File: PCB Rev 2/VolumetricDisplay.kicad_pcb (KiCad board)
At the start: 4 copper layers, 48.5 x 56 mm, 149 parts, among them J1 USB_C_Receptacle_USB2.0_16P, J2 Conn_ARM_SWD_TagConnect_TC2030, Q1 DMN32D2LDF, Q2 DMN32D2LDF, Q3 DMN32D2LDF, Q4 DMN32D2LDF, SW4 TS-1088-AR02016, SW5 TS-1088-AR02016, U2 NCP718xSN330, U3 RP2354B, U4 DRV8311S, U5 DRV5055A1xDBZxQ1, Y1 Abracon ABM8-272-T3

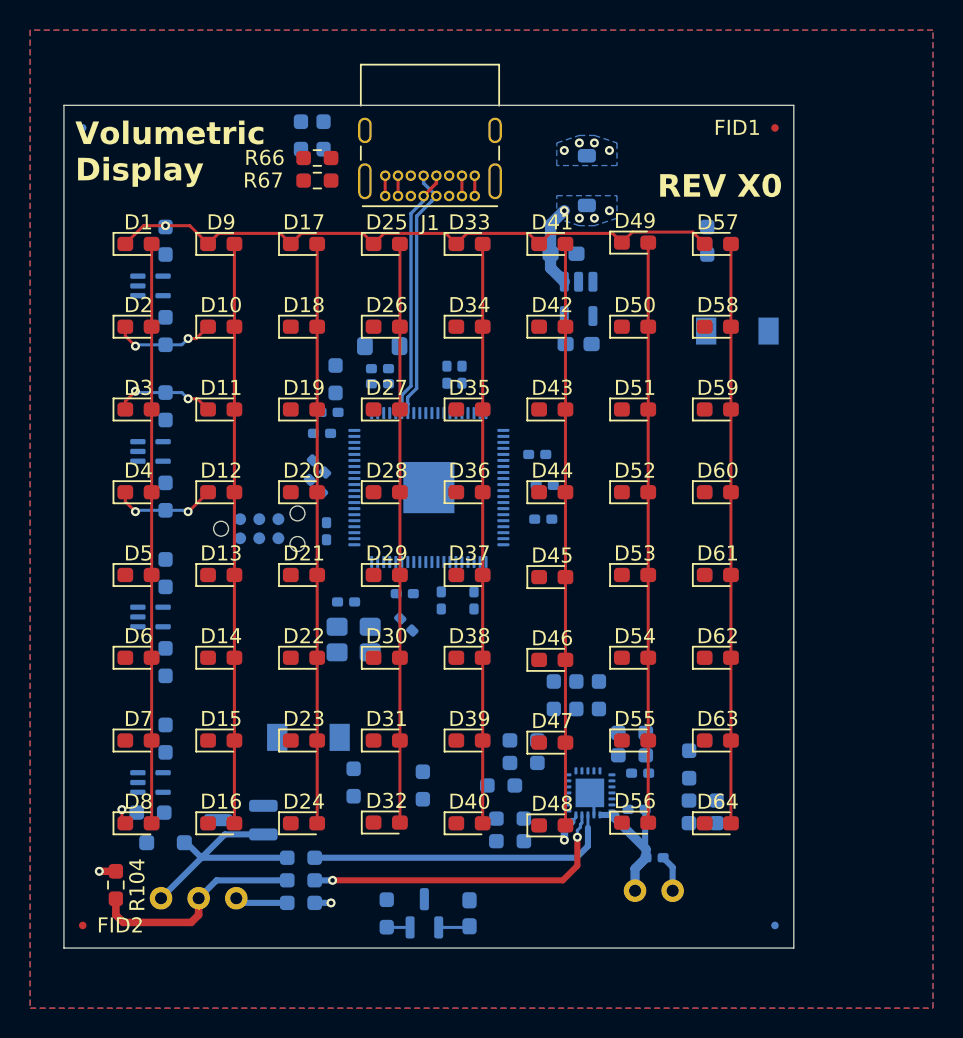
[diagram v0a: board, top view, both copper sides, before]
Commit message: Finished the LED array and worked on the voltage regulator
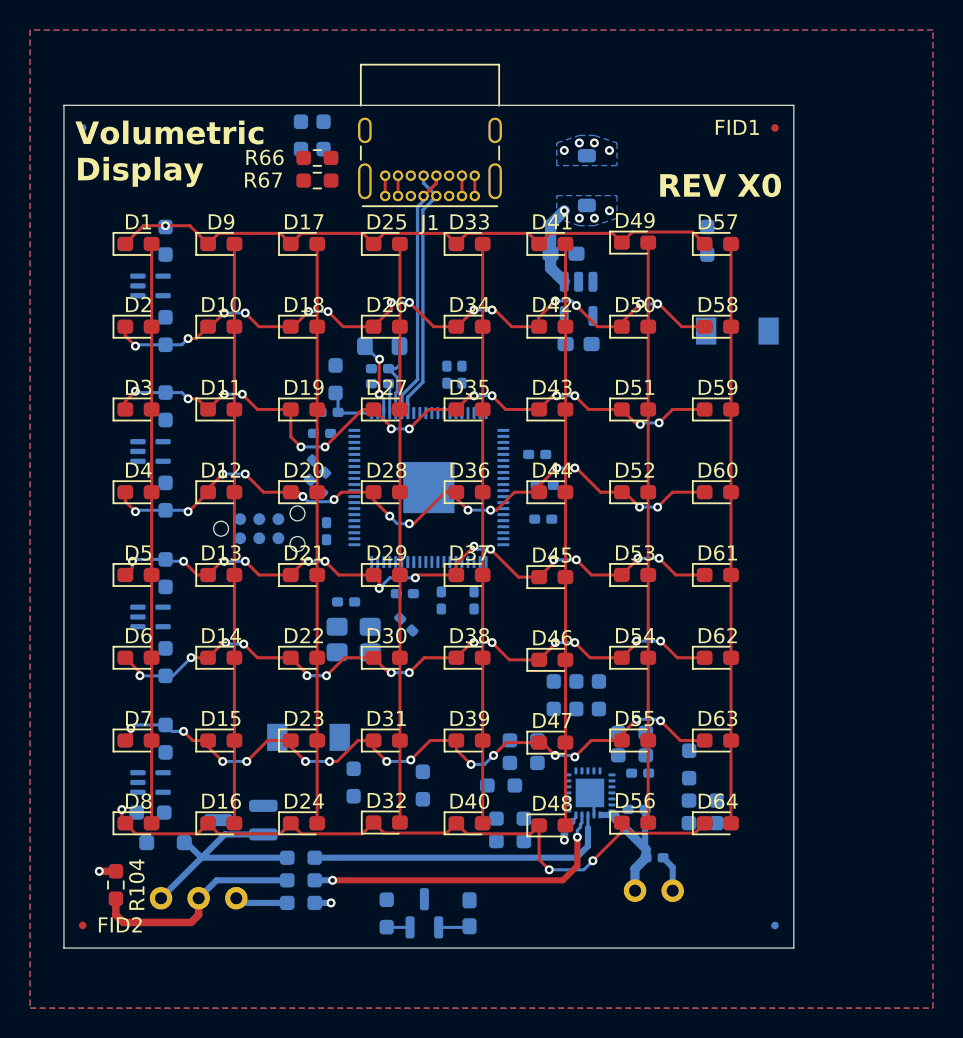
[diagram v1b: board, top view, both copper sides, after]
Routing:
- net Net-(D15-K): track 0.00 -> 47.7 mm, vias 0 -> 14
- net Net-(D13-K): track 0.00 -> 46.2 mm, vias 0 -> 14
- net Net-(D16-K): track 1.29 -> 47.4 mm, vias 1 -> 3
- net Net-(D14-K): track 0.00 -> 45.2 mm, vias 0 -> 14
- net Net-(D11-K): track 6.82 -> 47.2 mm, vias 2 -> 14
- net Net-(D12-K): track 7.00 -> 47.3 mm, vias 2 -> 14
- net Net-(D10-K): track 6.93 -> 47.3 mm, vias 2 -> 14
- net +1V1: track 0.00 -> 5.33 mm
- net Net-(U3-VREG_LX): track 0.00 -> 5.05 mm, vias 0 -> 2
- net Net-(U3-VREG_AVDD): track 0.00 -> 3.61 mm
- net 3V3: track 2.08 -> 4.07 mm
